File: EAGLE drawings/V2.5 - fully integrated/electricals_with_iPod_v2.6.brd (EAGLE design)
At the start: 61.9 x 56.8 mm, 47 parts, among them IC1 ATMEGA32U2-TQFP, Y1 16MHz

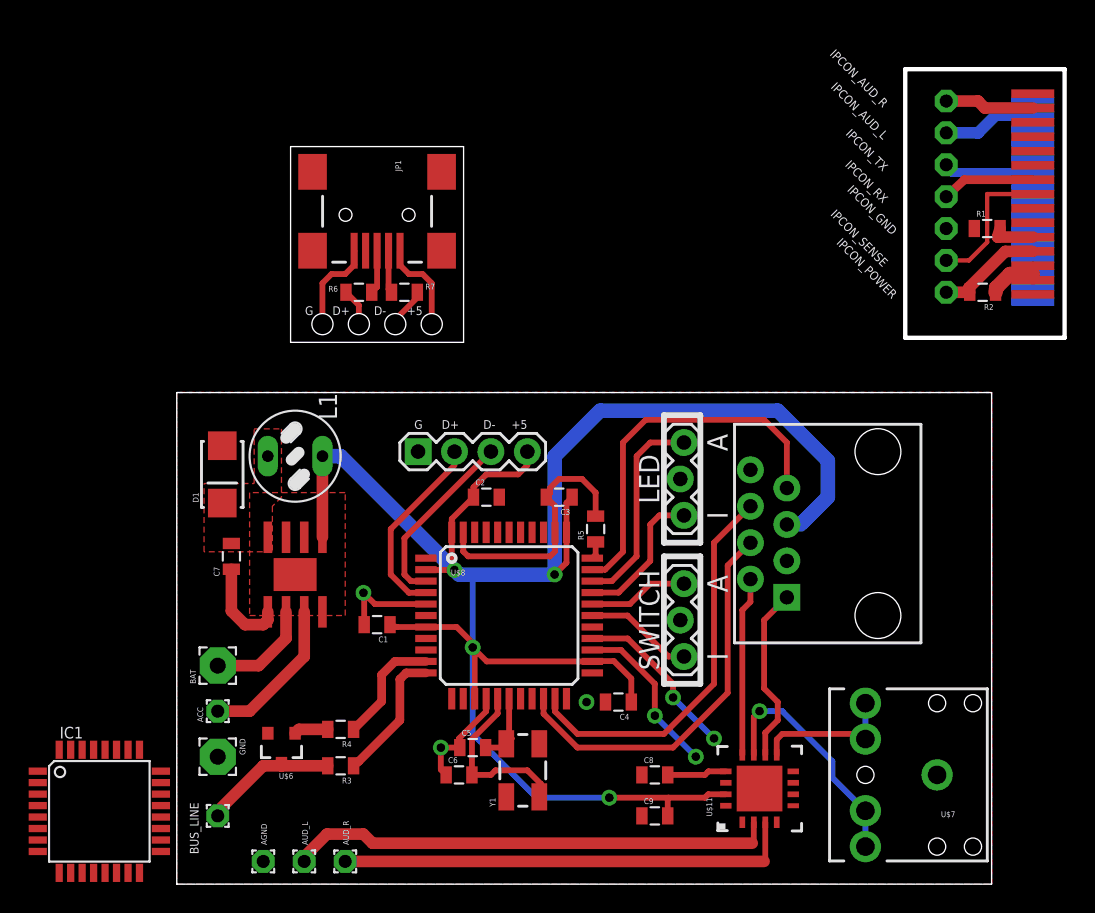
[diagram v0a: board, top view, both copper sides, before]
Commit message: Added v2.6 - smaller, 0603 passives, QFN mega*U4
Files edited with EAGLE 7.1.0
Split off v2.6
 - board about .25” shorter
 - 0603 passives
 - QFN package ATMega*U4
 - rearranged power supply
 - tweaked iPod connector board
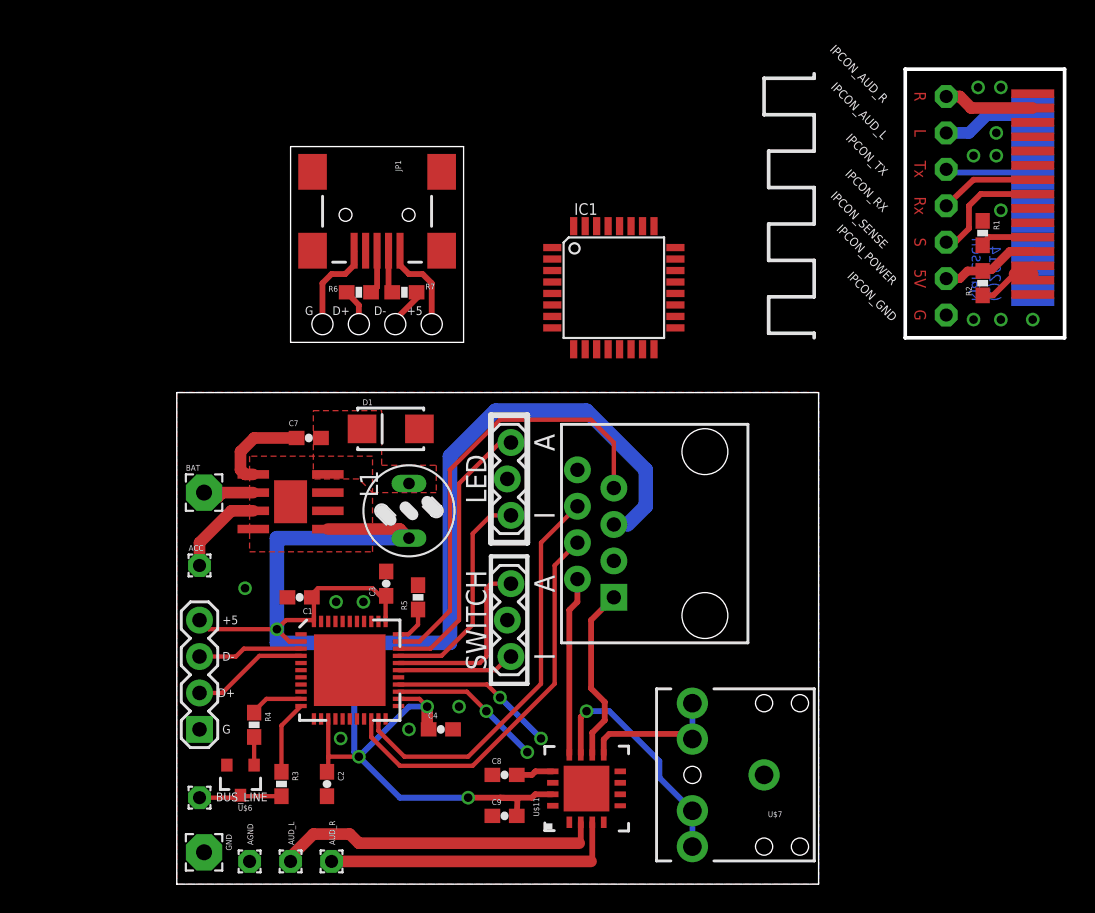
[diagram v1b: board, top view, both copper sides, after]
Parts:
- removed C5, C6: 10pF, SparkFun-Passives:0805
- removed Y1: 16MHz, SparkFun-FreqCtrl:CRYSTAL-SMD-5X3
- C1, C2, C3, C4, C7, C8, C9: device SparkFun-Passives:0805 -> SparkFun-Passives:0603-CAP
- R1, R2, R3, R4, R5, R6, R7: device SparkFun-Resistors:0805 -> SparkFun-Resistors:0603-RES
- U$8: value ATMEGA32U4TQFP -> ATMEGA32U4QFN; device SparkFun-DigitalIC:SPARKFUN-DIGITALIC_TQFP44 -> SparkFun-DigitalIC:SPARKFUN-DIGITALIC_QFN-44
- moved IC1 51.2 mm to (30.5, 41.6)
- moved JP6 24.6 mm to (1.59, 10.8), turned to 90 degrees
- moved C2 22.9 mm to (10.5, 6.99), turned to 270 degrees
- moved C3 13.5 mm to (14.6, 21.0), turned to 90 degrees
- moved R5 13.3 mm to (16.8, 20.0)
- moved C4 12.5 mm to (18.4, 10.8), turned to 0 degrees
- moved D1 12.2 mm to (14.9, 31.8), turned to 180 degrees
- moved BAT 12.1 mm to (1.91, 27.3), turned to 0 degrees
- moved U$3 12.1 mm to (36.8, 24.4)
- moved JP4 12.1 mm to (23.2, 21.0)
- moved JP5 12.1 mm to (23.2, 30.8)
- moved U$11 12.1 mm to (28.6, 6.67)
- moved U$7 12.1 mm to (41.0, 7.62)
- moved U$8 11.7 mm to (12.1, 14.9)
- moved C8 10.5 mm to (22.9, 7.62)
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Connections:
- removed net N$15: C5.2, U$8.17, Y1.3
- removed net N$28: C6.2, U$8.16, Y1.1
- net GND: no longer C5.1, C6.1
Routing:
- net GND: track 33.1 -> 0.00 mm, vias 3 -> 6
- net N$28: track 12.3 -> 0.00 mm
- net 5V: track 143.2 -> 131.5 mm
- net AUDIO_L: track 34.0 -> 22.9 mm
- net AUDIO_R: track 32.0 -> 20.9 mm
- net UC_INSEL_AUX: track 6.98 -> 12.9 mm
- net N$15: track 5.84 -> 0.00 mm
- net UC_IND_IPOD: track 10.1 -> 15.6 mm
- net USB_D-: track 12.8 -> 7.30 mm
- net UC_IND_AUX: track 14.5 -> 19.4 mm
- net UC_SENSE: track 26.2 -> 31.0 mm
- net N$1: track 10.7 -> 6.26 mm
- net MBUS_RX: track 8.10 -> 3.73 mm
- net USB_D+: track 12.4 -> 8.15 mm
- net MBUS_TX: track 9.39 -> 5.15 mm
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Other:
- outline, holes or cut-outs redrawn
- board text added: "(c)2014 kjanesch"
- board text added: "5V"
- board text added: "L"
- board text added: "R"
- board text added: "Rx"
- board text added: "S"
- board text added: "Tx"

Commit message: iPod breakout split from v2.6, new single-input board
The iPod connector board was pulled from V2.6 to send to OSHPark

v2.6 is pending revisions down from the ATMega 16U4 to [8|16|32]U2. May
shrink more.

A new board is in the works that can fit on the back of the stereo
connector, providing only an auxiliary input. Uses an ATTiny.
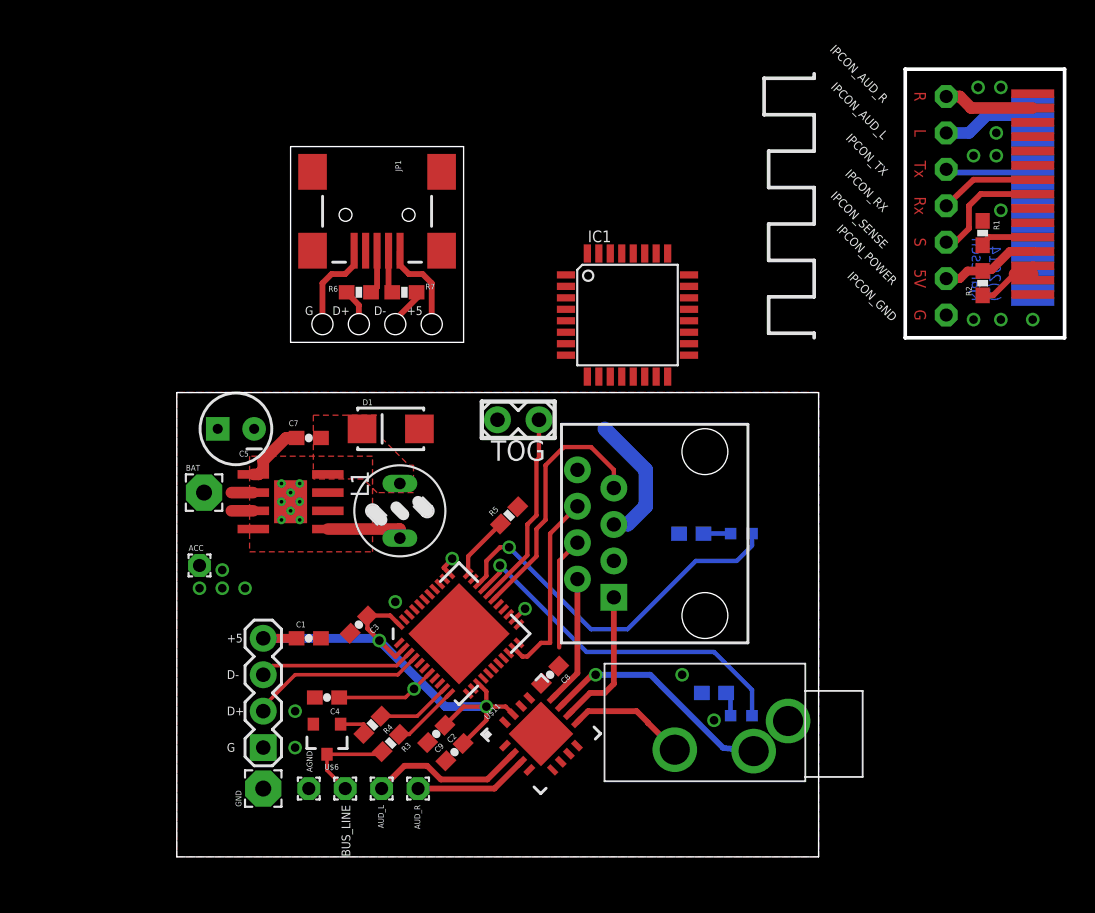
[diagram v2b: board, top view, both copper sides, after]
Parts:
- removed JP5: (no value), SparkFun-Connectors:1X03_LOCK
- added C5: (no value), SparkFun-Capacitors:CPOL-RADIAL-10UF-25V
- added LED1, LED2: (no value), SparkFun-LED:LED-0603
- added R8, R9: 330, SparkFun-Resistors:0603-RES
- JP4: device SparkFun-Connectors:1X03_LOCK -> SparkFun-Connectors:1X02_LOCK
- U$7: value AUDIO-JACK2PTH -> STEREO_JACK_SJ1-353XNG3NG; device SparkFun-Connectors:AUDIO-JACK -> personal:3.5MM_SJ1-353XNG
- moved JP4 11.6 mm to (25.1, 32.4), turned to 180 degrees
- moved BUS_LINE 10.2 mm to (11.7, 6.67)
- moved R5 8.54 mm to (23.2, 25.7), turned to 45 degrees
- moved C2 8.38 mm to (18.1, 10.5), turned to 225 degrees
- moved R4 8.25 mm to (13.7, 11.1), turned to 225 degrees
- moved C4 8.24 mm to (10.5, 13.0), turned to 180 degrees
- moved R3 8.14 mm to (14.9, 9.84), turned to 225 degrees
- moved AUD_L 8.13 mm to (14.3, 6.67), turned to 0 degrees
- moved U$8 8.03 mm to (19.7, 17.5), turned to 45 degrees
- moved AUD_R 7.89 mm to (16.8, 6.67), turned to 0 degrees
- moved C8 7.67 mm to (26.0, 14.6), turned to 225 degrees
- moved U$6 6.68 mm to (10.5, 10.2)
- moved AGND 6.55 mm to (9.21, 6.67)
- moved GND 6.07 mm to (6.03, 6.67), turned to 90 degrees
- moved C9 5.65 mm to (19.4, 9.21), turned to 45 degrees
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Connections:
- net UC_INSEL_AUX renamed UC_INSEL_TOG
- removed net UC_INSEL_IPOD: JP4.3, U$8.28
- new net N$15: LED1.C, R8.2
- new net N$16: LED2.C, R9.2
- net AUX_AUDIO_L: now also U$7.2; no longer U$7.RING, U$7.RSH
- net AUX_AUDIO_R: now also U$7.3; no longer U$7.TIP, U$7.TSH
- net GND: now also C5.2, R8.1, R9.1, U$7.1; no longer JP5.2, U$7.SLEEVE
- net N$2: now also C5.1
- net UC_IND_AUX: now also LED1.A; no longer JP5.1
- net UC_IND_IPOD: now also LED2.A; no longer JP5.3
- net UC_SENSE: now also U$8.28; no longer U$8.32
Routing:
- net 5V: track 131.5 -> 62.0 mm, vias 4 -> 5
- net UC_RX: track 27.8 -> 7.83 mm
- net UC_TX: track 28.4 -> 13.5 mm
- net UC_SENSE: track 31.0 -> 18.1 mm
- net AUDIO_R: track 20.9 -> 7.97 mm
- net AUDIO_L: track 22.9 -> 11.0 mm
- net UC_ENABLE_AUX: track 11.5 -> 0.00 mm, vias 2 -> 0
- net UC_ENABLE_IPOD: track 10.7 -> 0.00 mm, vias 2 -> 0
- net UC_IND_IPOD: track 15.6 -> 25.1 mm, vias 0 -> 1
- net UC_INSEL_IPOD: track 8.23 -> 0.00 mm
- net UC_IND_AUX: track 19.4 -> 26.4 mm, vias 0 -> 1
- net N$1: track 6.26 -> 1.53 mm
- net USB_D+: track 8.15 -> 12.3 mm
- net USB_D-: track 7.30 -> 10.8 mm
- net IPOD_AUDIO_L: track 12.5 -> 9.00 mm
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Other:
- board size 61.9 x 56.8 mm -> 61.9 x 54.9 mm
- board text added: "TOG"
- board text removed: "A"
- board text removed: "I"
- board text removed: "LED"
- board text removed: "SWITCH"

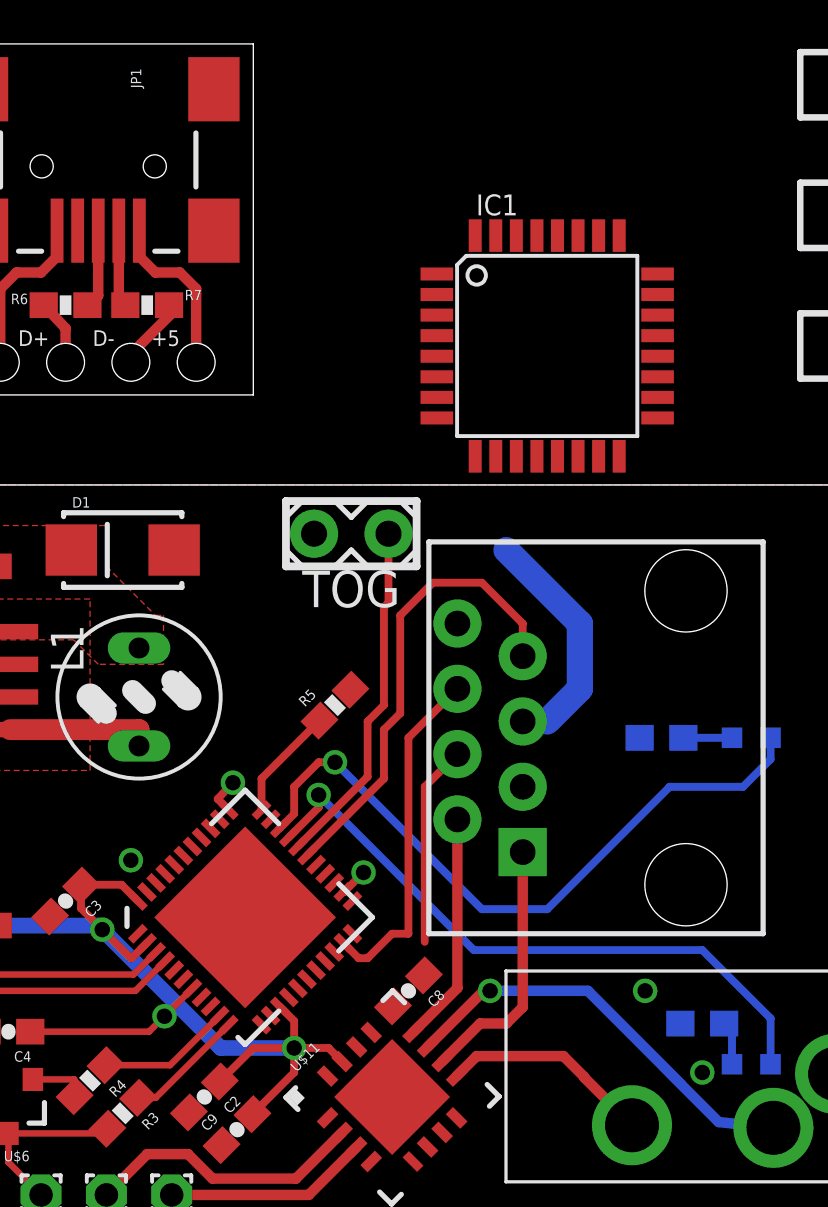
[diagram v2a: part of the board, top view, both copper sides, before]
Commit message: Updated aux-only board, preparing to switch to 32/16/8U2
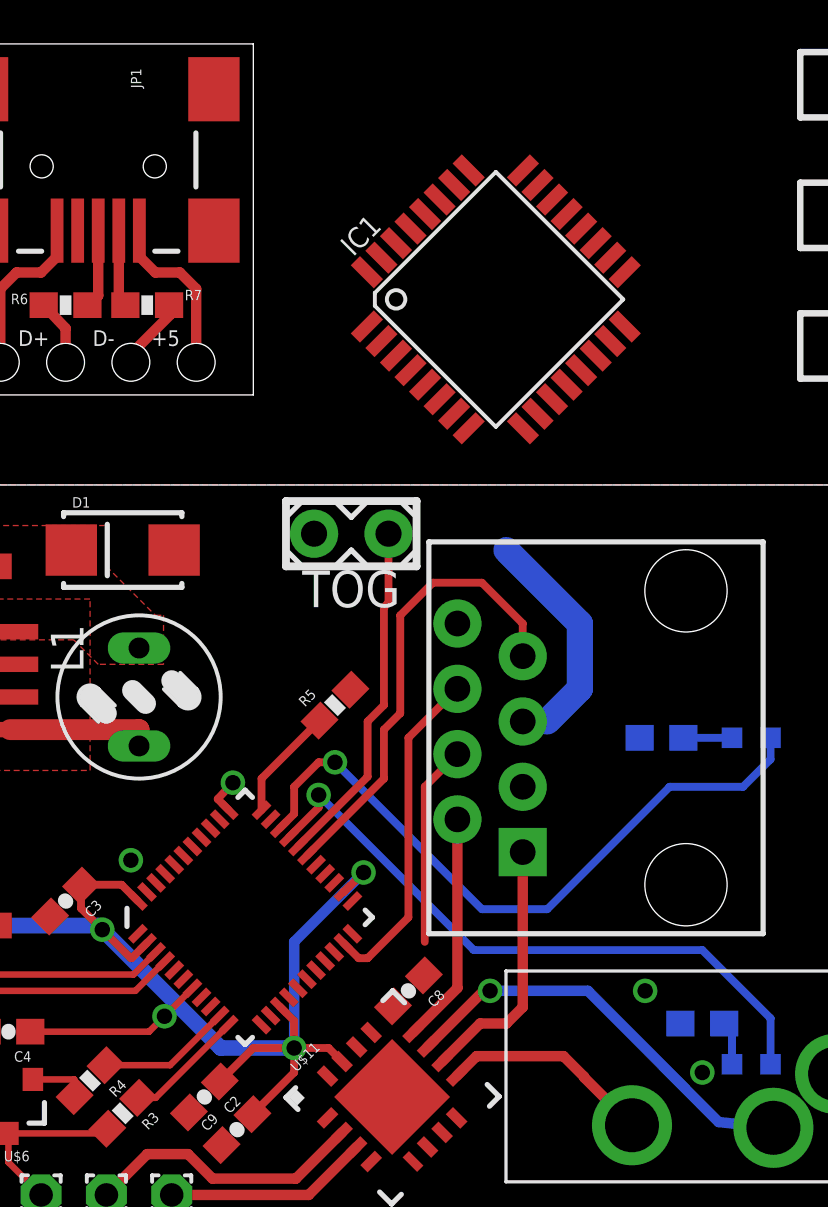
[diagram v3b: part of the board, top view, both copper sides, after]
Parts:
- U$8: value ATMEGA32U4QFN -> ATMEGA32U4QFN2; device SparkFun-DigitalIC:SPARKFUN-DIGITALIC_QFN-44 -> SparkFun-DigitalIC:SPARKFUN-DIGITALIC_QFN-44-NOPAD
- moved IC1 2.70 mm to (29.4, 41.5), turned to 45 degrees
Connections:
- new net N$17: IC1.28, IC1.3
- new net N$18: IC1.32, IC1.4
- new net N$23: IC1.18
- new net N$24: IC1.19
- new net N$25: IC1.20
- net UC_RX: now also IC1.8
- net UC_TX: now also IC1.9
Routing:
- net 5V: track 62.0 -> 70.9 mm
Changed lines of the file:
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@@
 <element name="R4" library="SparkFun-Resistors" package="0603-RES" value="4.7k" x="13.6525" y="11.1125" rot="R225"/>
 <element name="U$3" library="SparkFun-Connectors" package="RJ45-8" value="RJ45-8PTH" x="36.83" y="24.4475" rot="R90"/>
-<element name="U$8" library="SparkFun-DigitalIC" package="SPARKFUN-DIGITALIC_QFN-44" value="ATMEGA32U4QFN" x="19.685" y="17.4625" smashed="yes" rot="R45">
+<element name="U$8" library="SparkFun-DigitalIC" package="SPARKFUN-DIGITALIC_QFN-44-NOPAD" value="ATMEGA32U4QFN2" x="19.685" y="17.4625" smashed="yes" rot="R45">
 <attribute name="VALUE" x="19.2907875" y="11.7367" size="0.6096" layer="27" rot="R135"/>
 </element>
@@
 <attribute name="VALUE" x="15.494" y="33.401" size="0.4064" layer="27"/>
 </element>
-<element name="IC1" library="adafruit" package="TQFP32-08" value="ATMEGA32U2-TQFP" x="31.4325" y="39.6875"/>
+<element name="IC1" library="adafruit" package="TQFP32-08" value="ATMEGA32U2-TQFP" x="29.43450625" y="41.49950625" rot="R45"/>
 <element name="U$11" library="personal" package="QFN-16" value="ISL54405IRTZ" x="25.4" y="10.4775" rot="R45"/>
 <element name="C8" library="SparkFun-Passives" package="0603-CAP" value="0.1µF" x="26.035" y="14.605" rot="R225"/>
@@
 <via x="35.2425" y="14.605" extent="1-16" drill="0.6" shape="octagon"/>
 <via x="37.465" y="11.43" extent="1-16" drill="0.6" shape="octagon"/>
-<wire x1="26.636040625" y1="15.206040625" x2="23.856928125" y2="18.09889375" width="0" layer="19" extent="1-1"/>
 </signal>
 <signal name="5V">
@@
 <wire x1="19.048603125" y1="21.634428125" x2="18.61678125" y2="22.06625" width="0.3048" layer="1"/>
 <wire x1="18.61678125" y1="22.06625" x2="19.20875" y2="22.70125" width="0.3048" layer="1"/>
-<wire x1="30.48" y1="25.0825" x2="31.4325" y2="25.0825" width="0" layer="19" extent="16-16"/>
+<wire x1="24.28875" y1="19.20875" x2="21.59" y2="16.51" width="0.4064" layer="16"/>
+<wire x1="21.59" y1="16.51" x2="21.59" y2="12.3825" width="0.4064" layer="16"/>
+<wire x1="31.4325" y1="25.0825" x2="30.48" y2="25.0825" width="0.4064" layer="16"/>
 <wire x1="24.28875" y1="19.20875" x2="30.48" y2="25.0825" width="0" layer="19" extent="1-1"/>
-<wire x1="21.0285" y1="13.997675" x2="23.503375" y2="18.452446875" width="0" layer="19" extent="1-1"/>
 <wire x1="19.048603125" y1="21.634428125" x2="15.51306875" y2="18.09889375" width="0" layer="19" extent="1-1"/>
 <wire x1="15.5575" y1="24.13" x2="18.61678125" y2="22.06625" width="0" layer="19" extent="1-1"/>
@@
 <wire x1="27.94" y1="23.8125" x2="26.67" y2="22.5425" width="0.3048" layer="1"/>
 <wire x1="26.67" y1="22.5425" x2="26.67" y2="16.51" width="0.3048" layer="1"/>
+<contactref element="IC1" pad="8"/>
+<wire x1="27.94" y1="23.8125" x2="28.379078125" y2="36.484278125" width="0" layer="19" extent="1-1"/>
 <wire x1="23.149821875" y1="16.118996875" x2="26.67" y2="16.51" width="0" layer="19" extent="1-1"/>
 </signal>
@@
 <contactref element="U$3" pad="6"/>
 <wire x1="27.94" y1="26.3525" x2="26.035" y2="24.4475" width="0.3048" layer="1"/>
-<wire x1="26.035" y1="24.4475" x2="26.035" y2="16.8275" width="0.3048" layer="1"/>
+<wire x1="26.035" y1="24.4475" x2="26.035" y2="17.4625" width="0.3048" layer="1"/>
 <wire x1="23.503375" y1="16.47255" x2="24.100925" y2="15.875" width="0.3048" layer="1"/>
 <wire x1="24.100925" y1="15.875" x2="24.4475" y2="15.875" width="0.3048" layer="1"/>
-<wire x1="24.4475" y1="15.875" x2="25.4" y2="16.8275" width="0.3048" layer="1"/>
-<wire x1="25.4" y1="16.8275" x2="26.035" y2="16.8275" width="0.3048" layer="1"/>
+<wire x1="24.4475" y1="15.875" x2="26.035" y2="17.4625" width="0.3048" layer="1"/>
+<contactref element="IC1" pad="9"/>
+<wire x1="27.94" y1="26.3525" x2="30.48993125" y2="36.484278125" width="0" layer="19" extent="1-1"/>
 </signal>
 <signal name="UC_IND_IPOD">
@@
 <contactref element="U$11" pad="13"/>
 <contactref element="C8" pad="2"/>
-<wire x1="25.43395625" y1="14.00395625" x2="24.586825" y2="12.987728125" width="0" layer="19" extent="1-1"/>
+<wire x1="24.586825" y1="12.987728125" x2="25.43395625" y2="14.00395625" width="0" layer="19" extent="1-1"/>
 </signal>
 <signal name="N$15">
@@
 <wire x1="38.62" y1="13.03" x2="38.62" y2="11.7475" width="0.3048" layer="16"/>
 </signal>
+<signal name="N$17">
+<contactref element="IC1" pad="28"/>
+<contactref element="IC1" pad="3"/>
+<wire x1="25.55065" y1="39.31270625" x2="26.682021875" y2="44.817675" width="0" layer="19" extent="1-1"/>
+</signal>
+<signal name="N$18">
+<contactref element="IC1" pad="4"/>
+<contactref element="IC1" pad="32"/>
+<wire x1="24.419278125" y1="42.55493125" x2="26.116334375" y2="38.747021875" width="0" layer="19" extent="1-1"/>
+</signal>
+<signal name="N$23">
+<contactref element="IC1" pad="18"/>
+</signal>
+<signal name="N$24">
+<contactref element="IC1" pad="19"/>
+</signal>
+<signal name="N$25">
+<contactref element="IC1" pad="20"/>
+</signal>
 </signals>
